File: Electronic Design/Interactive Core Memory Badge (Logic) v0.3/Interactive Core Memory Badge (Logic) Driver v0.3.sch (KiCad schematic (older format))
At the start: 64 parts, among them J1 SSW-116-22-F-S-VS‎, J2 SSW-116-22-F-S-VS‎, Q10 MMBT4401LT1G, Q11 MMBT4403LT1G, Q12 MMBT4401LT1G, Q13 MMBT4403LT1G, Q14 MMBT4401LT1G, Q15 MMBT4403LT1G, Q16 MMBT4401LT1G, Q17 MMBT4403LT1G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

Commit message: Board layout, PDFs for review
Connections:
- net SAO3_GPIO2: now reaches J2.16 (Pin_16)
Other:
- note added: "XT: 4\nXB :8\nLED MATRIX: 3\n (V+, SIGNAL, GND)\nSPARE: 1 (SAO3)\nTOTAL=16"
- note removed: "N/C"
- note removed: "XT: 4\nXB :8\nLED MATRIX: 3\n (V+, SIGNAL, GND)\nSPARE: 1\nTOTAL=16"
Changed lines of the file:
@@
 $EndComp
 Text Notes 1950 1400 0    50   ~ 0
-XT: 4\nXB :8\nLED MATRIX: 3\n    (V+, SIGNAL, GND)\nSPARE: 1\nTOTAL=16
+XT: 4\nXB :8\nLED MATRIX: 3\n    (V+, SIGNAL, GND)\nSPARE: 1 (SAO3)\nTOTAL=16
 Wire Wire Line
 	2450 2400 2550 2400
@@
 	2550 2500 2450 2500
 Wire Wire Line
-	2550 3100 2100 3100
+	2550 3100 1900 3100
 Text Notes 750  3350 0    50   ~ 0
 DIGITAL LOGIC GROUND
@@
 L power:GND #PWR?
 U 1 1 5E79F49F
-P 2100 3100
+P 1900 3150
 AR Path="/5D254AE8/5E79F49F" Ref="#PWR?"  Part="1"
 AR Path="/5E79F49F" Ref="#PWR?"  Part="1"
 AR Path="/5E755AC8/5E79F49F" Ref="#PWR0165"  Part="1"
-F 0 "#PWR0165" H 2100 2850 50  0001 C CNN
-F 1 "GND" H 2105 2925 50  0000 C CNN
-F 2 "" H 2100 3100 50  0001 C CNN
-F 3 "" H 2100 3100 50  0001 C CNN
-	1    2100 3100
+F 0 "#PWR0165" H 1900 2900 50  0001 C CNN
+F 1 "GND" H 1905 2975 50  0000 C CNN
+F 2 "" H 1900 3150 50  0001 C CNN
+F 3 "" H 1900 3150 50  0001 C CNN
+	1    1900 3150
 	1    0    0    -1
 $EndComp
@@
 L power:+VSW #PWR0122
 U 1 1 5E76A192
-P 2100 2850
-F 0 "#PWR0122" H 2100 2700 50  0001 C CNN
-F 1 "+VSW" H 2115 3025 50  0000 C CNN
-F 2 "" H 2100 2850 50  0001 C CNN
-F 3 "" H 2100 2850 50  0001 C CNN
-	1    2100 2850
+P 1900 2850
+F 0 "#PWR0122" H 1900 2700 50  0001 C CNN
+F 1 "+VSW" H 1915 3025 50  0000 C CNN
+F 2 "" H 1900 2850 50  0001 C CNN
+F 3 "" H 1900 2850 50  0001 C CNN
+	1    1900 2850
 	1    0    0    -1
 $EndComp
 Wire Wire Line
-	2100 2900 2100 2850
+	1900 2900 1900 2850
 Wire Wire Line
-	2100 2900 2550 2900
-Text Notes 2350 3200 0    50   ~ 0
-N/C
+	1900 2900 2550 2900
 Wire Wire Line
 	1450 7100 1900 7100
@@
 Wire Wire Line
 	3800 7200 3900 7200
+Text GLabel 2550 3200 0    50   BiDi ~ 0
+SAO3_GPIO2
+Wire Wire Line
+	1900 3100 1900 3150
 $EndSCHEMATC

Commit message: Schematic review tweaks
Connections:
- net 3V3_100mA is gone; now on net VMEM: J1.11 (Pin_11)
- net LED_MATRIX_+VSW renamed LED_MATRIX_+VSW_SIG
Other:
- moved on the sheet: J1, J2
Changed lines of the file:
@@
 Wire Wire Line
 	1200 4450 2400 4450
+Text GLabel 2450 2300 0    50   Output ~ 0
+XB3
+Text GLabel 2450 2200 0    50   Output ~ 0
+XB2
+Text GLabel 2450 2100 0    50   Output ~ 0
+XB1
+Text GLabel 2450 2000 0    50   Output ~ 0
+XB0
 Text GLabel 2450 2400 0    50   Output ~ 0
-XB3
-Text GLabel 2450 2300 0    50   Output ~ 0
-XB2
-Text GLabel 2450 2200 0    50   Output ~ 0
-XB1
-Text GLabel 2450 2100 0    50   Output ~ 0
-XB0
+XB4
 Text GLabel 2450 2500 0    50   Output ~ 0
-XB4
+XB5
 Text GLabel 2450 2600 0    50   Output ~ 0
-XB5
+XB6
 Text GLabel 2450 2700 0    50   Output ~ 0
-XB6
-Text GLabel 2450 2800 0    50   Output ~ 0
 XB7
-Text GLabel 2450 2000 0    50   Output ~ 0
+Text GLabel 2450 1900 0    50   Output ~ 0
 XT0-4
-Text GLabel 2450 1900 0    50   Output ~ 0
+Text GLabel 2450 1800 0    50   Output ~ 0
 XT1-5
-Text GLabel 2450 1800 0    50   Output ~ 0
+Text GLabel 2450 1700 0    50   Output ~ 0
 XT2-6
-Text GLabel 2450 1700 0    50   Output ~ 0
+Text GLabel 2450 1600 0    50   Output ~ 0
 XT3-7
 Wire Wire Line
+	2450 1600 2550 1600
+Wire Wire Line
 	2450 1700 2550 1700
 Wire Wire Line
@@
 Wire Wire Line
 	2450 1900 2550 1900
-Wire Wire Line
-	2450 2000 2550 2000
-Text GLabel 1450 1800 2    50   Output ~ 0
+Text GLabel 1400 1700 2    50   Output ~ 0
 YL1
-Text GLabel 1450 1700 2    50   Output ~ 0
+Text GLabel 1400 1600 2    50   Output ~ 0
 YL0
-Text GLabel 1450 1900 2    50   Output ~ 0
+Text GLabel 1400 1800 2    50   Output ~ 0
 YL2
-Text GLabel 1450 2000 2    50   Output ~ 0
+Text GLabel 1400 1900 2    50   Output ~ 0
 YL3
-Text GLabel 1450 2400 2    50   Output ~ 0
+Text GLabel 1400 2300 2    50   Output ~ 0
 YL7
 Wire Wire Line
-	1400 2100 1400 2300
-Wire Wire Line
-	1400 2300 1450 2300
-Wire Wire Line
-	1450 1700 800  1700
-Wire Wire Line
-	1450 2000 800  2000
-Wire Wire Line
-	1450 2100 1400 2100
-Wire Wire Line
-	1400 2100 800  2100
-Connection ~ 1400 2100
-Wire Wire Line
-	1350 2400 1450 2400
-Wire Wire Line
-	1350 2200 1350 2400
-Wire Wire Line
-	1450 2200 1350 2200
-Text Notes 600  1400 0    50   ~ 0
+	1350 2000 1350 2200
+Wire Wire Line
+	1350 2200 1400 2200
+Wire Wire Line
+	1400 1600 750  1600
+Wire Wire Line
+	1400 1900 750  1900
+Wire Wire Line
+	1400 2000 1350 2000
+Wire Wire Line
+	1350 2000 750  2000
+Connection ~ 1350 2000
+Wire Wire Line
+	1300 2300 1400 2300
+Wire Wire Line
+	1300 2100 1300 2300
+Wire Wire Line
+	1400 2100 1300 2100
+Text Notes 550  1300 0    50   ~ 0
 YL: 6\nSENSE: 2\nSPARE: 2\nGND, 3V3: 2\nMHS: 4 (hall switches)\nTOTAL=16
 Wire Wire Line
-	1350 2200 800  2200
-Connection ~ 1350 2200
-Wire Wire Line
-	2450 2800 2550 2800
+	1300 2100 750  2100
+Connection ~ 1300 2100
 Wire Wire Line
 	2450 2700 2550 2700
+Wire Wire Line
+	2450 2600 2550 2600
 $Comp
 L Connector:Conn_01x16_Female J2
 U 1 1 5E78B5ED
-P 2750 2400
-F 0 "J2" H 2100 3350 50  0000 C CNN
-F 1 "SSW-116-22-F-S-VS‎" H 2400 3250 50  0000 C CNN
-F 2 "Connector_PinHeader_2.54mm:PinHeader_1x16_P2.54mm_Vertical_SMD_and_TH_Pin1Left" H 2750 2400 50  0001 C CNN
-F 3 "~" H 2750 2400 50  0001 C CNN
-	1    2750 2400
+P 2750 2300
+F 0 "J2" H 1950 3250 50  0000 C CNN
+F 1 "SSW-116-22-F-S-VS‎" H 2350 3150 50  0000 C CNN
+F 2 "Connector_PinHeader_2.54mm:PinHeader_1x16_P2.54mm_Vertical_SMD_and_TH_Pin1Left" H 2750 2300 50  0001 C CNN
+F 3 "~" H 2750 2300 50  0001 C CNN
+	1    2750 2300
 	1    0    0    -1
 $EndComp
@@
 L Connector:Conn_01x16_Female J1
 U 1 1 5E78B5F3
-P 600 2400
-F 0 "J1" H 550 3350 50  0000 C CNN
-F 1 "SSW-116-22-F-S-VS‎" H 250 3250 50  0000 C CNN
-F 2 "Connector_PinHeader_2.54mm:PinHeader_1x16_P2.54mm_Vertical_SMD_and_TH_Pin1Left" H 600 2400 50  0001 C CNN
-F 3 "~" H 600 2400 50  0001 C CNN
-	1    600  2400
+P 550 2300
+F 0 "J1" H 500 3250 50  0000 C CNN
+F 1 "SSW-116-22-F-S-VS‎" H 100 3150 50  0000 C CNN
+F 2 "Connector_PinHeader_2.54mm:PinHeader_1x16_P2.54mm_Vertical_SMD_and_TH_Pin1Left" H 550 2300 50  0001 C CNN
+F 3 "~" H 550 2300 50  0001 C CNN
+	1    550  2300
 	-1   0    0    -1
 $EndComp
-Text Notes 1950 1400 0    50   ~ 0
+Text Notes 1900 1300 0    50   ~ 0
 XT: 4\nXB :8\nLED MATRIX: 3\n    (V+, SIGNAL, GND)\nSPARE: 1 (SAO3)\nTOTAL=16
 Wire Wire Line
-	2450 2400 2550 2400
-Wire Wire Line
-	2450 2600 2550 2600
-Text GLabel 900  2300 2    50   Input ~ 0
+	2450 2300 2550 2300
+Wire Wire Line
+	2450 2500 2550 2500
+Text GLabel 850  2200 2    50   Input ~ 0
 SENSE1
-Text GLabel 900  2400 2    50   Input ~ 0
+Text GLabel 850  2300 2    50   Input ~ 0
 SENSE2
 Wire Wire Line
-	900  2400 800  2400
-Text GLabel 2500 3000 0    50   Input ~ 0
-LED_MATRIX_+VSW
-Wire Wire Line
-	2500 3000 2550 3000
+	850  2300 750  2300
+Text GLabel 2500 2900 0    50   Input ~ 0
+LED_MATRIX_+VSW_SIG
+Wire Wire Line
+	2500 2900 2550 2900
 $Comp
 L power:GNDD #PWR0164
 U 1 1 5E78B651
-P 1600 3050
-F 0 "#PWR0164" H 1600 2800 50  0001 C CNN
-F 1 "GNDD" H 1604 2895 50  0000 C CNN
-F 2 "" H 1600 3050 50  0001 C CNN
-F 3 "" H 1600 3050 50  0001 C CNN
-	1    1600 3050
-	1    0    0    -1
-$EndComp
-Text GLabel 850  2900 2    50   Output ~ 0
+P 1550 3050
+F 0 "#PWR0164" H 1550 2800 50  0001 C CNN
+F 1 "GNDD" H 1554 2895 50  0000 C CNN
+F 2 "" H 1550 3050 50  0001 C CNN
+F 3 "" H 1550 3050 50  0001 C CNN
+	1    1550 3050
+	1    0    0    -1
+$EndComp
+Text GLabel 800  2800 2    50   Output ~ 0
 HALL_SWITCH_1
-Text GLabel 850  3000 2    50   Output ~ 0
+Text GLabel 800  2900 2    50   Output ~ 0
 HALL_SWITCH_2
-Text GLabel 850  3100 2    50   Output ~ 0
+Text GLabel 800  3000 2    50   Output ~ 0
 HALL_SWITCH_3
-Text GLabel 850  3200 2    50   Output ~ 0
+Text GLabel 800  3100 2    50   Output ~ 0
 HALL_SWITCH_4
 Wire Wire Line
-	1600 2800 1600 3050
-Wire Wire Line
-	800  2700 900  2700
-Wire Wire Line
-	800  2800 1600 2800
-Wire Wire Line
-	850  3000 800  3000
-Wire Wire Line
-	850  3200 800  3200
+	1550 2700 1550 3050
+Wire Wire Line
+	750  2600 850  2600
+Wire Wire Line
+	750  2700 1550 2700
+Wire Wire Line
+	800  2900 750  2900
+Wire Wire Line
+	800  3100 750  3100
+Wire Wire Line
+	2550 2000 2450 2000
 Wire Wire Line
 	2550 2100 2450 2100
@@
 	2550 2200 2450 2200
 Wire Wire Line
-	2550 2300 2450 2300
-Wire Wire Line
-	2550 2500 2450 2500
-Wire Wire Line
-	2550 3100 1900 3100
-Text Notes 750  3350 0    50   ~ 0
+	2550 2400 2450 2400
+Wire Wire Line
+	2550 3000 1900 3000
+Text Notes 550  3300 0    50   ~ 0
 DIGITAL LOGIC GROUND
 Text Notes 4200 7750 0    50   ~ 0
@@
 L power:GND #PWR?
 U 1 1 5E79F49F
-P 1900 3150
+P 1900 3050
 AR Path="/5D254AE8/5E79F49F" Ref="#PWR?"  Part="1"
 AR Path="/5E79F49F" Ref="#PWR?"  Part="1"
 AR Path="/5E755AC8/5E79F49F" Ref="#PWR0165"  Part="1"
-F 0 "#PWR0165" H 1900 2900 50  0001 C CNN
-F 1 "GND" H 1905 2975 50  0000 C CNN
-F 2 "" H 1900 3150 50  0001 C CNN
-F 3 "" H 1900 3150 50  0001 C CNN
-	1    1900 3150
-	1    0    0    -1
-$EndComp
-Text GLabel 900  2700 2    50   Input ~ 0
-3V3_100mA
-Wire Wire Line
-	800  1800 1450 1800
-Wire Wire Line
-	800  1900 1450 1900
-Wire Wire Line
-	800  2300 900  2300
-Wire Wire Line
-	800  2900 850  2900
-Wire Wire Line
-	800  3100 850  3100
-Text Notes 2200 3350 0    50   ~ 0
+F 0 "#PWR0165" H 1900 2800 50  0001 C CNN
+F 1 "GND" H 1905 2875 50  0000 C CNN
+F 2 "" H 1900 3050 50  0001 C CNN
+F 3 "" H 1900 3050 50  0001 C CNN
+	1    1900 3050
+	1    0    0    -1
+$EndComp
+Text GLabel 850  2600 2    50   Input ~ 0
+3V3_800mA
+Wire Wire Line
+	750  1700 1400 1700
+Wire Wire Line
+	750  1800 1400 1800
+Wire Wire Line
+	750  2200 850  2200
+Wire Wire Line
+	750  2800 800  2800
+Wire Wire Line
+	750  3000 800  3000
+Text Notes 2000 3300 0    50   ~ 0
 SYSTEM POWER GROUND
 Text Notes 550  750  0    118  ~ 0
@@
 L power:+VSW #PWR0122
 U 1 1 5E76A192
-P 1900 2850
-F 0 "#PWR0122" H 1900 2700 50  0001 C CNN
-F 1 "+VSW" H 1915 3025 50  0000 C CNN
-F 2 "" H 1900 2850 50  0001 C CNN
-F 3 "" H 1900 2850 50  0001 C CNN
-	1    1900 2850
-	1    0    0    -1
-$EndComp
-Wire Wire Line
-	1900 2900 1900 2850
-Wire Wire Line
-	1900 2900 2550 2900
+P 1900 2750
+F 0 "#PWR0122" H 1900 2600 50  0001 C CNN
+F 1 "+VSW" H 1915 2925 50  0000 C CNN
+F 2 "" H 1900 2750 50  0001 C CNN
+F 3 "" H 1900 2750 50  0001 C CNN
+	1    1900 2750
+	1    0    0    -1
+$EndComp
+Wire Wire Line
+	1900 2800 1900 2750
+Wire Wire Line
+	1900 2800 2550 2800
 Wire Wire Line
 	1450 7100 1900 7100
@@
 Wire Wire Line
 	1250 7400 1250 7500
-Text GLabel 900  2500 2    50   BiDi ~ 0
+Text GLabel 850  2400 2    50   BiDi ~ 0
 I2C_CLOCK
-Text GLabel 900  2600 2    50   BiDi ~ 0
+Text GLabel 850  2500 2    50   BiDi ~ 0
 I2C_DATA
-Text GLabel 1450 2300 2    50   Output ~ 0
+Text GLabel 1400 2200 2    50   Output ~ 0
 YL6
-Text GLabel 1450 2200 2    50   Output ~ 0
+Text GLabel 1400 2100 2    50   Output ~ 0
 YL5
-Text GLabel 1450 2100 2    50   Output ~ 0
+Text GLabel 1400 2000 2    50   Output ~ 0
 YL4
 Wire Wire Line
-	800  2500 900  2500
-Wire Wire Line
-	800  2600 900  2600
+	750  2400 850  2400
+Wire Wire Line
+	750  2500 850  2500
 Wire Wire Line
 	4200 6850 5300 6850
 Wire Wire Line
 	3800 7200 3900 7200
-Text GLabel 2550 3200 0    50   BiDi ~ 0
+Text GLabel 2550 3100 0    50   BiDi ~ 0
 SAO3_GPIO2
 Wire Wire Line
-	1900 3100 1900 3150
+	1900 3000 1900 3050
 $EndSCHEMATC

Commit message: Schematic refinement
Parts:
- removed TP2: VMEM, TestPoint:TestPoint_THTPad_D1.7mm_Drill1.0mm, symbol Connector:TestPoint
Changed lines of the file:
@@
 Sheet 2 5
 Title "Core 64 - Core Array Driver"
-Date "2020-03-15"
+Date "2020-04-24"
 Rev "0.3"
 Comp "Andy Geppert - Machine Ideas, LLC"
@@
 	1900 2800 2550 2800
 Wire Wire Line
-	1450 7100 1900 7100
-Wire Wire Line
 	1050 7100 1250 7100
-Connection ~ 1450 7100
-Wire Wire Line
-	1450 7100 1450 7000
-$Comp
-L Connector:TestPoint TP?
-U 1 1 5E8ED577
-P 1450 7000
-AR Path="/5D254AE8/5E8ED577" Ref="TP?"  Part="1"
-AR Path="/5E8ED577" Ref="TP?"  Part="1"
-AR Path="/5E755AC8/5E8ED577" Ref="TP2"  Part="1"
-F 0 "TP2" H 1508 7118 50  0000 L CNN
-F 1 "VMEM" H 1508 7027 50  0000 L CNN
-F 2 "TestPoint:TestPoint_THTPad_D1.7mm_Drill1.0mm" H 1650 7000 50  0001 C CNN
-F 3 "~" H 1650 7000 50  0001 C CNN
-	1    1450 7000
-	1    0    0    -1
-$EndComp
 $Comp
 L Device:CP1_Small C?
@@
 PLACE\nCAPACITOR\nNEAR\nCORE DRIVERS
 Connection ~ 1250 7100
-Wire Wire Line
-	1250 7100 1450 7100
 $Comp
 L power:GND #PWR?
@@
 Wire Wire Line
 	1900 3000 1900 3050
+Wire Wire Line
+	1250 7100 1900 7100
 $EndSCHEMATC

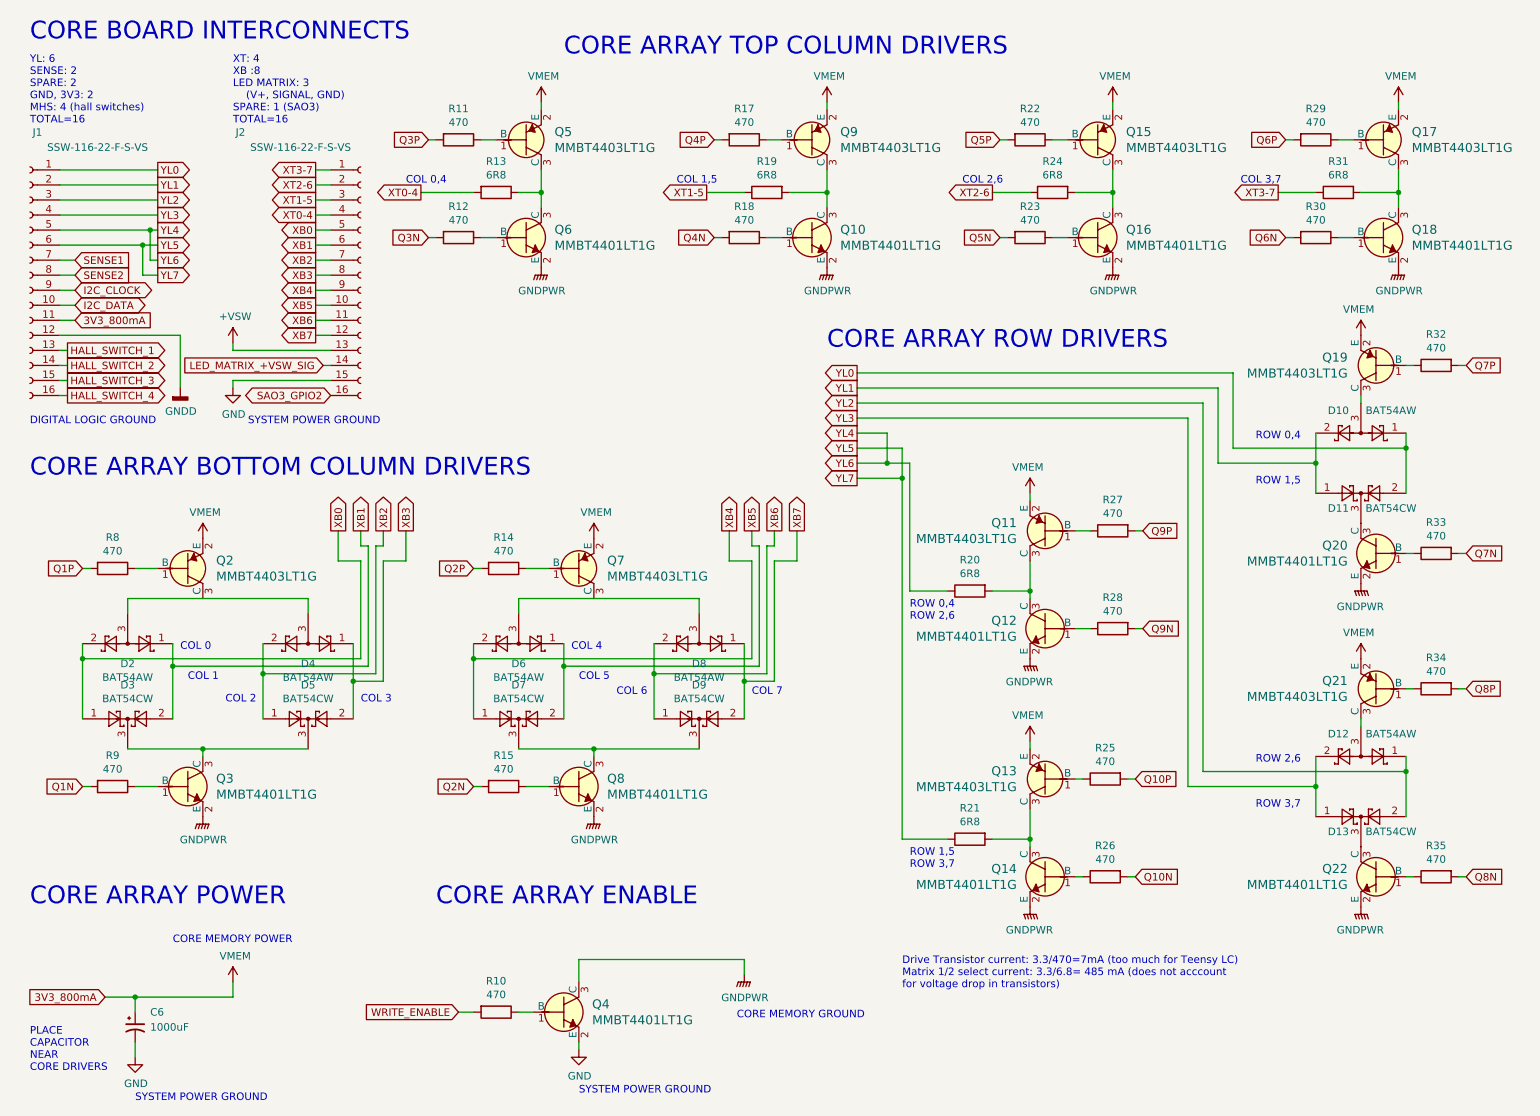
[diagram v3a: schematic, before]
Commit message: Logic board layout power routing
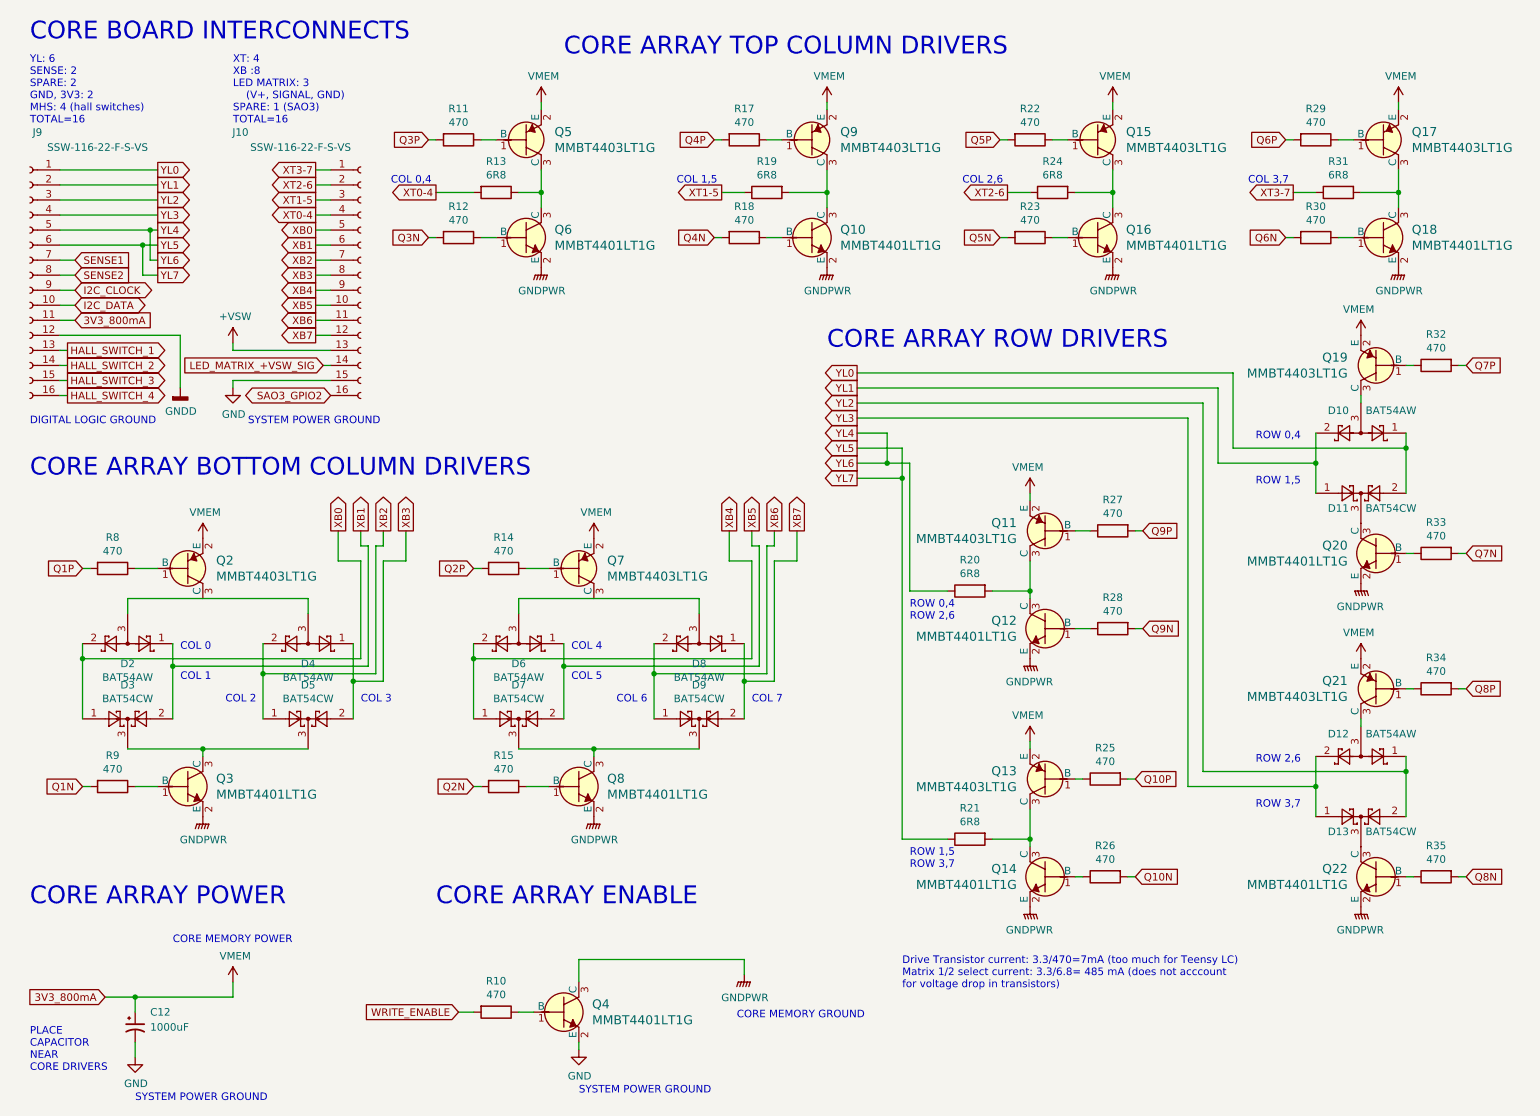
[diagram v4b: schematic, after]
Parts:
- C12: renamed from C6; footprint Capacitor_SMD:CP_Elec_8x10 -> Capacitor_SMD:CP_Elec_10x10
- renumbered J2 to J10, J1 to J9
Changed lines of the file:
@@
 Wire Wire Line
 	3950 1150 3950 1200
-Text GLabel 3150 1750 0    50   Output ~ 0
+Text GLabel 3250 1750 0    50   Output ~ 0
 XT0-4
-Text GLabel 5050 1750 0    50   Output ~ 0
+Text GLabel 5150 1750 0    50   Output ~ 0
 XT1-5
-Text GLabel 6950 1750 0    50   Output ~ 0
+Text GLabel 7050 1750 0    50   Output ~ 0
 XT2-6
-Text GLabel 8850 1750 0    50   Output ~ 0
+Text GLabel 8950 1750 0    50   Output ~ 0
 XT3-7
 $Comp
@@
 	9650 1750 9650 1850
 Wire Wire Line
-	8850 1750 9100 1750
-Wire Wire Line
-	7200 1750 6950 1750
+	8950 1750 9100 1750
+Wire Wire Line
+	7200 1750 7050 1750
 $Comp
 L Device:R R24
@@
 $EndComp
 Wire Wire Line
-	5050 1750 5300 1750
+	5150 1750 5300 1750
 Wire Wire Line
 	3800 1750 3950 1750
@@
 	3950 1750 3950 1850
 Wire Wire Line
-	3150 1750 3500 1750
+	3250 1750 3500 1750
 Wire Wire Line
 	9650 1600 9650 1750
@@
 Text Notes 6350 7050 0    50   ~ 0
 Drive Transistor current: 3.3/470=7mA (too much for Teensy LC)\nMatrix 1/2 select current: 3.3/6.8= 485 mA (does not acccount \nfor voltage drop in transistors)
-Text Notes 3050 1700 0    50   ~ 0
+Text Notes 2950 1700 0    50   ~ 0
 COL 0,4
 Text Notes 4850 1700 0    50   ~ 0
@@
 Text Notes 6750 1700 0    50   ~ 0
 COL 2,6
-Text Notes 8600 1700 0    50   ~ 0
+Text Notes 8650 1700 0    50   ~ 0
 COL 3,7
 Text Notes 1550 4800 0    50   ~ 0
 COL 0
-Text Notes 1600 5000 0    50   ~ 0
+Text Notes 1550 5000 0    50   ~ 0
 COL 1
 Text Notes 1850 5150 0    50   ~ 0
@@
 Text Notes 4150 4800 0    50   ~ 0
 COL 4
-Text Notes 4200 5000 0    50   ~ 0
+Text Notes 4150 5000 0    50   ~ 0
 COL 5
-Text Notes 4450 5100 0    50   ~ 0
+Text Notes 4450 5150 0    50   ~ 0
 COL 6
-Text Notes 5350 5100 0    50   ~ 0
+Text Notes 5350 5150 0    50   ~ 0
 COL 7
 Text Notes 6400 4600 0    50   ~ 0
@@
 	2450 2600 2550 2600
 $Comp
-L Connector:Conn_01x16_Female J2
+L Connector:Conn_01x16_Female J10
 U 1 1 5E78B5ED
 P 2750 2300
-F 0 "J2" H 1950 3250 50  0000 C CNN
+F 0 "J10" H 1950 3250 50  0000 C CNN
 F 1 "SSW-116-22-F-S-VS‎" H 2350 3150 50  0000 C CNN
 F 2 "Connector_PinHeader_2.54mm:PinHeader_1x16_P2.54mm_Vertical_SMD_and_TH_Pin1Left" H 2750 2300 50  0001 C CNN
@@
 $EndComp
 $Comp
-L Connector:Conn_01x16_Female J1
+L Connector:Conn_01x16_Female J9
 U 1 1 5E78B5F3
 P 550 2300
-F 0 "J1" H 500 3250 50  0000 C CNN
+F 0 "J9" H 500 3250 50  0000 C CNN
 F 1 "SSW-116-22-F-S-VS‎" H 100 3150 50  0000 C CNN
 F 2 "Connector_PinHeader_2.54mm:PinHeader_1x16_P2.54mm_Vertical_SMD_and_TH_Pin1Left" H 550 2300 50  0001 C CNN
@@
 AR Path="/5E755787/5E91F406" Ref="C?"  Part="1"
 AR Path="/5E755AC8/5D2551FF/5E91F406" Ref="C?"  Part="1"
-AR Path="/5E755AC8/5E91F406" Ref="C6"  Part="1"
-F 0 "C6" H 1350 7400 50  0000 L CNN
+AR Path="/5E755AC8/5E91F406" Ref="C12"  Part="1"
+F 0 "C12" H 1350 7400 50  0000 L CNN
 F 1 "1000uF" H 1350 7300 50  0000 L CNN
-F 2 "Capacitor_SMD:CP_Elec_8x10" H 1250 7300 50  0001 C CNN
+F 2 "Capacitor_SMD:CP_Elec_10x10" H 1250 7300 50  0001 C CNN
 F 3 "~" H 1250 7300 50  0001 C CNN
 	1    1250 7300
